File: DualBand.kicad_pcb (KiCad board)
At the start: 2 copper layers, 70.4 x 42.6 mm, 47 parts, among them J1 Conn_01x02_Male, J2 Conn_01x03_Male, J3 Conn_01x01_Male, J4 Conn_01x10_Male, J5 Conn_01x03_Male, J6 Conn_01x10_Male, J7 Conn_01x03_Male, P2 AD8402ARUZ1, SW1 SW_Push, U1 LM7322QMAX/NOPB, U2 MSP430FR2311IPW20R, U3 LMH6703MA/NOPB, U4 LMH6703MA/NOPB

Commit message: Generated Gerbers
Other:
- board text added: "Chris Dietsch & Lonnie Souder II"
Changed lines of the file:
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@@
-(kicad_pcb (version 4) (host pcbnew 4.0.7)
+(kicad_pcb (version 4) (host pcbnew 4.0.4-stable)
   (general
     (links 118)
     (no_connects 0)
-    (area 97.714999 97.953689 172.160001 167.8)
+    (area 97.79 98.053689 172.160001 167.8)
     (thickness 1.6)
-    (drawings 7)
+    (drawings 8)
     (tracks 718)
     (zones 0)
@@
     (visible_elements 7FFFFFFF)
     (pcbplotparams
-      (layerselection 0x00030_80000001)
-      (usegerberextensions false)
+      (layerselection 0x010f0_80000001)
+      (usegerberextensions true)
       (excludeedgelayer true)
       (linewidth 0.100000)
@@
       (psa4output false)
       (plotreference true)
-      (plotvalue true)
+      (plotvalue false)
       (plotinvisibletext false)
       (padsonsilk false)
@@
       (outputformat 1)
       (mirror false)
-      (drillshape 1)
+      (drillshape 0)
       (scaleselection 1)
       (outputdirectory ""))
@@
     )
   )
+  (gr_text "Chris Dietsch & Lonnie Souder II" (at 158.2 141.2) (layer F.SilkS)
+    (effects (font (size 1 1) (thickness 0.25)))
+  )
   (gr_line (start 101.6635 100.965) (end 172.085 100.965) (angle 90) (layer Edge.Cuts) (width 0.15))

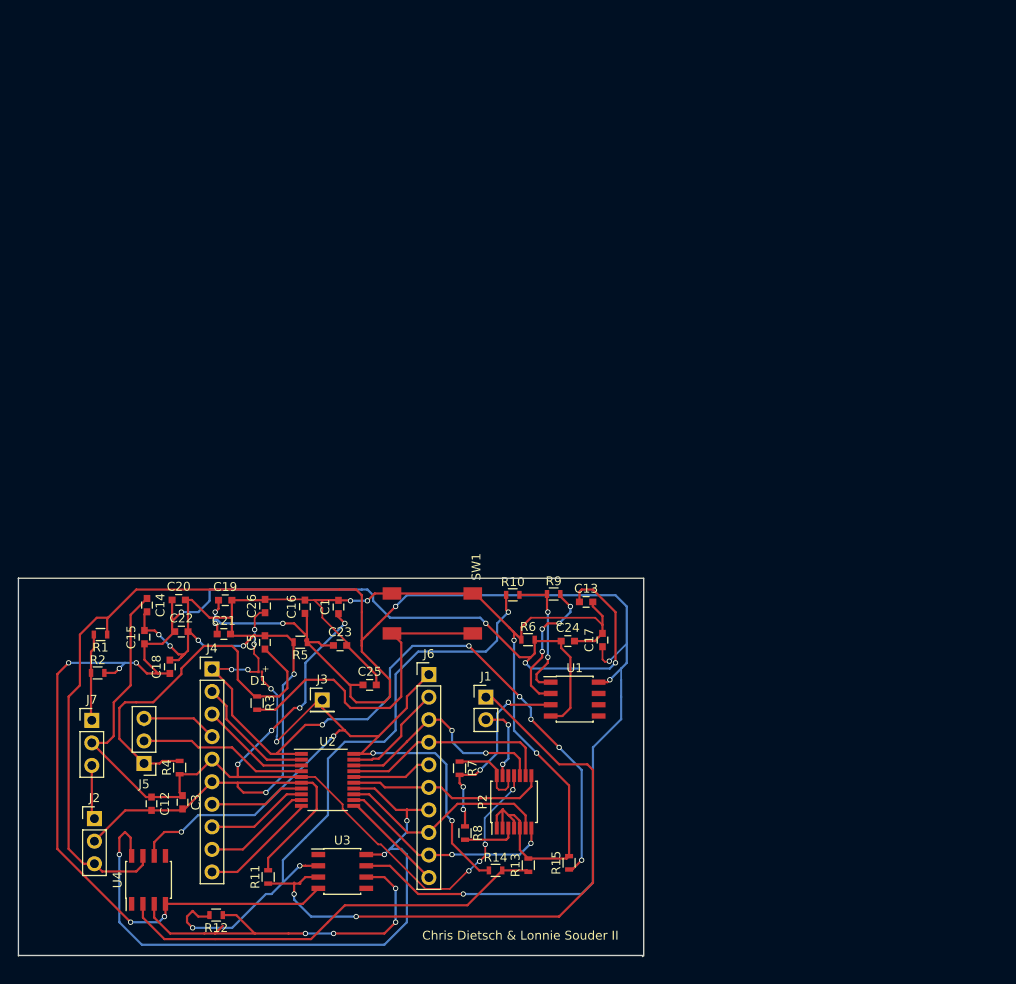
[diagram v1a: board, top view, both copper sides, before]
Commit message: Recreates PCB based on new layout
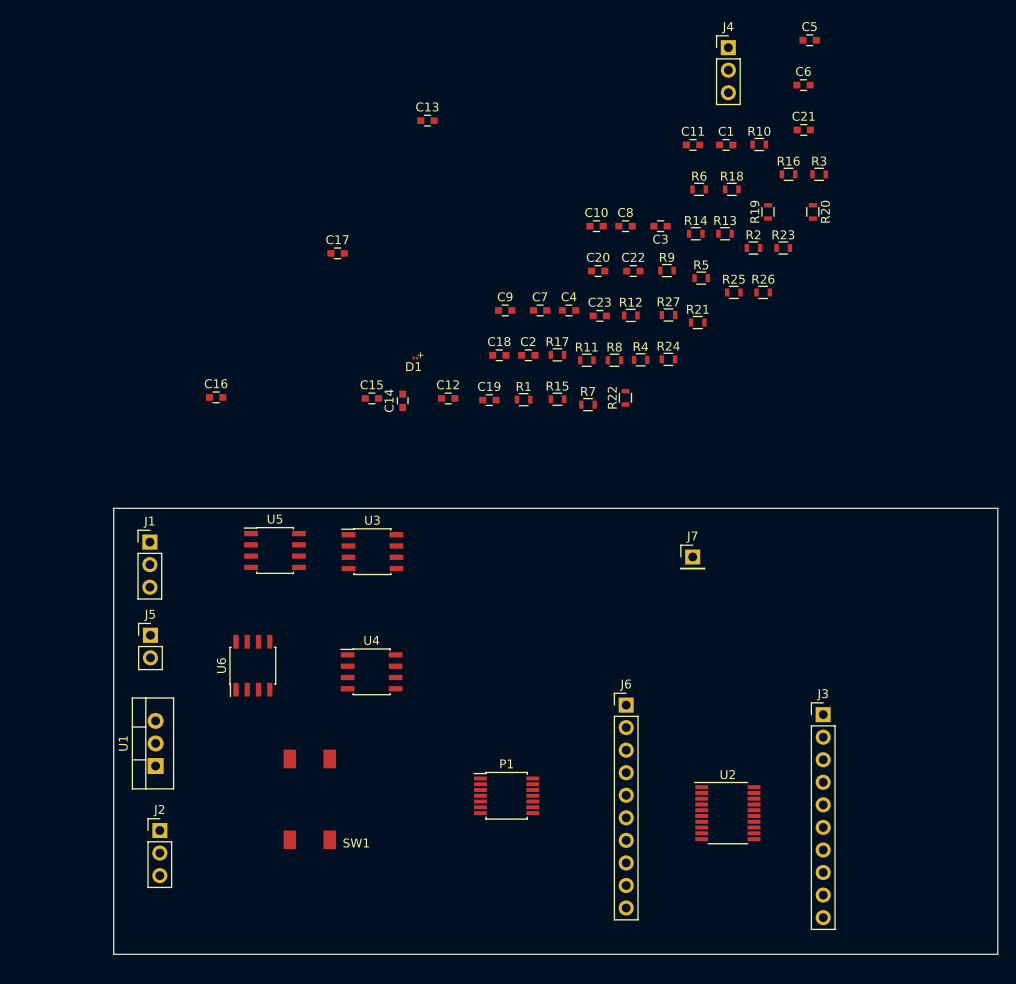
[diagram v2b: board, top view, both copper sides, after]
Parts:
- removed C24, C25: 0.01u, Capacitors_SMD:C_0603
- removed C26: 0.1u, Capacitors_SMD:C_0603
- removed P2: AD8402ARUZ1, Housings_SSOP:TSSOP-14_4.4x5mm_Pitch0.65mm
- added C10: 1u, Capacitors_SMD:C_0603, F.Cu at (166.8, 61.3)
- added C11: 1u, Capacitors_SMD:C_0603, F.Cu at (177.6, 52.2)
- added C2: 1u, Capacitors_SMD:C_0603, F.Cu at (159.1, 75.9)
- added C4: 10u, Capacitors_SMD:C_0603, F.Cu at (163.7, 70.8)
- added C6: 1u, Capacitors_SMD:C_0603, F.Cu at (190.1, 45.4)
- added C7: 1u, Capacitors_SMD:C_0603, F.Cu at (160.4, 70.8)
- added C8: 1u, Capacitors_SMD:C_0603, F.Cu at (170.0, 61.3)
- added C9: 0.01u, Capacitors_SMD:C_0603, F.Cu at (156.5, 70.8)
- added P1: AD8402ARUZ1, Housings_SSOP:TSSOP-14_4.4x5mm_Pitch0.65mm, F.Cu at (156.6, 125.5)
- added R16: 820, Resistors_SMD:R_0603, F.Cu at (188.4, 55.5)
- added R17: 10k, Resistors_SMD:R_0603, F.Cu at (162.4, 75.8)
- added R18: 100, Resistors_SMD:R_0603, F.Cu at (182.0, 57.2)
- added R19: 10k, Resistors_SMD:R_0603, F.Cu at (186.1, 59.7)
- added R20: 1k, Resistors_SMD:R_0603, F.Cu at (191.1, 59.7)
- added R21: 1k, Resistors_SMD:R_0603, F.Cu at (178.2, 72.2)
- added R22: 287, Resistors_SMD:R_0603, F.Cu at (170.0, 80.6)
- added R23: 2.4k, Resistors_SMD:R_0603, F.Cu at (187.8, 63.8)
- added R24: 470, Resistors_SMD:R_0603, F.Cu at (174.9, 76.3)
- added R25: 100, Resistors_SMD:R_0603, F.Cu at (182.2, 68.8)
- added R26: 220, Resistors_SMD:R_0603, F.Cu at (185.5, 68.8)
- added R27: 10k, Resistors_SMD:R_0603, F.Cu at (174.9, 71.3)
- added U5: LMH6703MA/NOPB, Housings_SOIC:SOIC-8_3.9x4.9mm_Pitch1.27mm, F.Cu at (130.6, 97.8)
- added U6: LMH6703MA/NOPB, Housings_SOIC:SOIC-8_3.9x4.9mm_Pitch1.27mm, F.Cu at (128.1, 110.8)
- C1: value 1u -> 100n
- C12, C19, C22: value 1u -> 0.01u
- C15, C17, C20, C21: value 0.01u -> 1u
- C23: value 1u -> 0.1u
- J1: value Conn_01x02_Male -> Conn_01x03_Male; footprint Pin_Headers:Pin_Header_Straight_1x02_Pitch2.54mm -> Pin_Headers:Pin_Header_Straight_1x03_Pitch2.54mm
- J3: value Conn_01x01_Male -> Conn_01x10_Male; footprint Pin_Headers:Pin_Header_Straight_1x01_Pitch2.54mm -> Pin_Headers:Pin_Header_Straight_1x10_Pitch2.54mm
- J4: value Conn_01x10_Male -> Conn_01x03_Male; footprint Pin_Headers:Pin_Header_Straight_1x10_Pitch2.54mm -> Pin_Headers:Pin_Header_Straight_1x03_Pitch2.54mm
- J5: value Conn_01x03_Male -> Conn_01x02_Male; footprint Pin_Headers:Pin_Header_Straight_1x03_Pitch2.54mm -> Pin_Headers:Pin_Header_Straight_1x02_Pitch2.54mm
- J7: value Conn_01x03_Male -> Conn_01x01_Male; footprint Pin_Headers:Pin_Header_Straight_1x03_Pitch2.54mm -> Pin_Headers:Pin_Header_Straight_1x01_Pitch2.54mm
- R1: value 12k -> 10k
- R10: value 100 -> 10
- R11: value 75 -> 10
- R12: value 287 -> 24k
- R13: value 100 -> 24k
- R14: value 220 -> 250
- R15: value 10k -> 820
- R2: value 78.7k -> 10k
- R3: value 10k -> 3.9k
- R4: value 10k -> 1k
- R5, R6: value 10k -> 510k
- R7: value 3k -> 1.3k
- R8: value 10 -> R
- R9: value 250 -> R
- U1: value LM7322QMAX/NOPB -> LD1117V33; footprint Housings_SOIC:SOIC-8_3.9x4.9mm_Pitch1.27mm -> TO_SOT_Packages_THT:TO-220-3_Vertical
- moved C5 91.5 mm to (190.8, 40.4), turned to 0 degrees
- moved J4 91.0 mm to (181.6, 41.2)
- moved R2 88.0 mm to (184.5, 63.8)
- moved R3 86.9 mm to (191.8, 55.5), turned to 0 degrees
- moved C21 86.5 mm to (190.1, 50.5)
- moved C3 84.3 mm to (174.0, 61.3), turned to 180 degrees
- moved R12 82.1 mm to (170.6, 71.4), turned to 0 degrees
- moved R14 75.2 mm to (177.9, 62.2)
- moved R13 74.5 mm to (181.2, 62.2), turned to 0 degrees
- moved J7 70.1 mm to (177.6, 98.6)
- moved R4 69.3 mm to (171.7, 76.4), turned to 0 degrees
- moved R11 68.4 mm to (165.7, 76.4), turned to 0 degrees
- moved C1 67.9 mm to (181.4, 52.2), turned to 0 degrees
- moved C22 65.1 mm to (170.9, 66.4)
- moved R5 61.0 mm to (178.6, 67.2), turned to 0 degrees
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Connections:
- C1 pad 1: /DVCC -> +9V
- C13 pad 1: /-4.5V -> +9V
- C14 pad 1: /DVCC -> +9V
- C15 pad 1: /-4.5V -> Net-(C15-Pad1)
- C15 pad 2: GND -> Net-(C15-Pad2)
- C16 pad 1: +9V -> Net-(C16-Pad1)
- C16 pad 2: GND -> /DataSignalIn
- C17 pad 1: +9V -> Net-(C17-Pad1)
- C18 pad 1: /-4.5V -> +9V
- C20 pad 1: /-4.5V -> Net-(C20-Pad1)
- C20 pad 2: GND -> Net-(C20-Pad2)
- C22 pad 1: /-4.5V -> +9V
- C23 pad 1: +9V -> Net-(C23-Pad1)
- C3 pad 2: GND -> Net-(C3-Pad2)
- D1 pad 1: Net-(C26-Pad1) -> Net-(C23-Pad1)
- J1 pad 1: /DataSignalIn -> +3V3
- J1 pad 2: /PowerSignalIn -> GND
- J2 pad 1: +3V3 -> Net-(C4-Pad1)
- J2 pad 2: GND -> /DVCC
- J2 pad 3: +9V -> +3V3
- J3 pad 1: /DataOut -> Net-(C23-Pad1)
- J4 pad 1: Net-(C26-Pad1) -> Net-(C5-Pad1)
- J4 pad 3: Net-(J4-Pad3) -> Net-(J3-Pad4)
- J5 pad 1: Net-(C5-Pad1) -> /DataSignalIn
- J7 pad 1: Net-(J7-Pad1) -> /DataOut
- R1 pad 1: +9V -> Net-(C5-Pad1)
- R1 pad 2: Net-(J7-Pad1) -> Net-(R1-Pad2)
- R10 pad 1: Net-(R10-Pad1) -> Net-(P1-Pad12)
- R10 pad 2: Net-(R10-Pad2) -> Net-(C11-Pad2)
- R11 pad 1: /DataSignalIn -> Net-(C11-Pad2)
- R11 pad 2: GND -> Net-(P1-Pad3)
- R12 pad 1: Net-(R12-Pad1) -> +9V
- R12 pad 2: Net-(R10-Pad1) -> Net-(C11-Pad1)
- R13 pad 1: Net-(R13-Pad1) -> Net-(C11-Pad1)
- R14 pad 1: /DataOut -> Net-(C15-Pad2)
- R14 pad 2: Net-(R13-Pad1) -> Net-(R14-Pad2)
- R15 pad 1: Net-(C26-Pad1) -> +9V
- R15 pad 2: GND -> Net-(C15-Pad1)
- R2 pad 1: Net-(J7-Pad1) -> /DVCC
- R2 pad 2: /-4.5V -> Net-(C5-Pad1)
- R3 pad 1: Net-(C5-Pad1) -> Net-(J5-Pad2)
- R3 pad 2: Net-(R3-Pad2) -> Net-(C6-Pad2)
- R4 pad 1: /DVCC -> Net-(C6-Pad2)
- R4 pad 2: Net-(C5-Pad1) -> GND
- R5 pad 2: GND -> Net-(C6-Pad1)
- R6 pad 1: GND -> Net-(C6-Pad1)
- R6 pad 2: /-4.5V -> GND
- R7 pad 1: Net-(P2-Pad12) -> Net-(C8-Pad2)
- R8 pad 1: Net-(R7-Pad2) -> +9V
- R8 pad 2: Net-(P2-Pad3) -> Net-(C8-Pad1)
- R9 pad 1: Net-(R10-Pad2) -> Net-(C8-Pad1)
- R9 pad 2: Net-(R9-Pad2) -> GND
- SW1 pad 2: Net-(R3-Pad2) -> Net-(R1-Pad2)
- U1 pad 1: Net-(R10-Pad2) -> GND
- U1 pad 2: Net-(R9-Pad2) -> Net-(C4-Pad1)
- U1 pad 3: Net-(R7-Pad2) -> +9V
- U2 pad 1: Net-(C26-Pad1) -> Net-(C23-Pad1)
- U2 pad 10: Net-(J4-Pad10) -> Net-(J3-Pad10)
- U2 pad 2: Net-(J4-Pad2) -> Net-(J3-Pad2)
- U2 pad 3: Net-(J4-Pad3) -> Net-(J3-Pad3)
- U2 pad 4: Net-(J5-Pad2) -> Net-(J4-Pad2)
- U2 pad 7: Net-(J4-Pad7) -> Net-(J3-Pad7)
- U2 pad 8: Net-(J4-Pad8) -> Net-(J3-Pad8)
- U2 pad 9: Net-(J4-Pad9) -> Net-(J3-Pad9)
- U3 pad 2: Net-(R10-Pad1) -> Net-(R7-Pad2)
- U3 pad 3: /DataSignalIn -> Net-(C6-Pad1)
- U3 pad 4: /-4.5V -> GND
- U3 pad 6: Net-(R12-Pad1) -> Net-(C8-Pad2)
- U4 pad 2: Net-(R13-Pad1) -> Net-(R14-Pad2)
- U4 pad 3: Net-(R12-Pad1) -> Net-(C11-Pad1)
- U4 pad 4: /-4.5V -> GND
- U4 pad 6: /DataOut -> Net-(C15-Pad2)
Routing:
- net +9V: track 222.5 -> 0.00 mm, vias 7 -> 0
- net GND: track 219.5 -> 0.00 mm, vias 10 -> 0
- net /-4.5V: track 168.8 -> 0.00 mm, vias 9 -> 0
- net /DVCC: track 112.7 -> 0.00 mm, vias 8 -> 0
- net /DataOut: track 91.0 -> 0.00 mm, vias 6 -> 0
- net Net-(C26-Pad1): track 88.6 -> 0.00 mm, vias 10 -> 0
- net /~SD: track 75.4 -> 0.00 mm, vias 3 -> 0
- net /DataSignalIn: track 72.4 -> 0.00 mm, vias 2 -> 0
- net Net-(R10-Pad1): track 71.8 -> 0.00 mm, vias 3 -> 0
- net Net-(R13-Pad1): track 49.2 -> 0.00 mm
- net Net-(R12-Pad1): track 44.1 -> 0.00 mm, vias 4 -> 0
- net Net-(C5-Pad1): track 43.8 -> 0.00 mm
- net Net-(R3-Pad2): track 37.0 -> 0.00 mm
- net Net-(J6-Pad3): track 25.3 -> 0.00 mm, vias 2 -> 0
- net Net-(J6-Pad9): track 24.8 -> 0.00 mm, vias 2 -> 0
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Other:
- board size 70.4 x 42.6 mm -> 99.6 x 50.2 mm
- net class Default: clearance 0.1 -> 0.2; trace_width 0.2 -> 0.25
- net class Diode removed
- rule trace_clearance: 0.1 -> 0.2
- board text removed: "Chris Dietsch & Lonnie Souder II"

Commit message: Revised PCB
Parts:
- added C24: 1u, Capacitors_SMD:C_0603, F.Cu at (138.4, 113.5)
- moved J4 96.8 mm to (164.8, 136.6), turned to 270 degrees
- moved R3 89.4 mm to (122.7, 112.1)
- moved R10 77.5 mm to (163.8, 126.7), turned to 270 degrees
- moved R20 74.4 mm to (167.6, 130.3)
- moved C3 74.3 mm to (155.6, 133.3)
- moved R6 74.2 mm to (165.7, 130.3), turned to 90 degrees
- moved C4 70.8 mm to (117.8, 124.8)
- moved C21 70.4 mm to (155.3, 111.7), turned to 270 degrees
- moved C10 70.1 mm to (155.7, 130.5), turned to 180 degrees
- moved R2 68.1 mm to (158.5, 126.8), turned to 90 degrees
- moved R26 68.0 mm to (158.8, 131.3), turned to 270 degrees
- moved R19 66.8 mm to (163.2, 122.5), turned to 180 degrees
- moved C5 66.8 mm to (159.4, 99.4), turned to 90 degrees
- moved C6 66.7 mm to (166.2, 107.7), turned to 270 degrees
- moved R25 65.0 mm to (161.2, 130.3), turned to 90 degrees
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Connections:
- C3 pad 2: Net-(C3-Pad2) -> GND
- R26 pad 1: /DataOut -> Net-(C24-Pad2)
- U6 pad 6: /DataOut -> Net-(C24-Pad2)
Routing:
- net GND: track 0.00 -> 219.4 mm, vias 0 -> 15
- net +9V: track 0.00 -> 138.3 mm, vias 0 -> 13
- net Net-(C17-Pad1): track 0.00 -> 131.8 mm, vias 0 -> 8
- net Net-(J6-Pad8): track 0.00 -> 117.4 mm, vias 0 -> 4
- net Net-(C6-Pad2): track 0.00 -> 116.4 mm, vias 0 -> 8
- net Net-(C8-Pad1): track 0.00 -> 109.1 mm, vias 0 -> 4
- net /DVCC: track 0.00 -> 91.7 mm, vias 0 -> 8
- net Net-(C6-Pad1): track 0.00 -> 80.9 mm, vias 0 -> 6
- net Net-(J6-Pad3): track 0.00 -> 65.9 mm, vias 0 -> 3
- net Net-(C11-Pad1): track 0.00 -> 63.4 mm, vias 0 -> 6
- net /~SD: track 0.00 -> 62.7 mm, vias 0 -> 4
- net Net-(C23-Pad1): track 0.00 -> 61.0 mm, vias 0 -> 4
- net Net-(R17-Pad1): track 0.00 -> 55.9 mm, vias 0 -> 6
- net Net-(C15-Pad1): track 0.00 -> 48.5 mm, vias 0 -> 4
- net Net-(C5-Pad1): track 0.00 -> 47.0 mm, vias 0 -> 6
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- added copper zone on B.Cu, net GND
- added copper zone on F.Cu, net GND
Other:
- board size 99.6 x 50.2 mm -> 68.5 x 53 mm
- net class Default: clearance 0.2 -> 0.05
- net class Large added: clearance 0.05, trace_width 0.45, via_dia 0.6, via_drill 0.45
- rule trace_clearance: 0.2 -> 0.05
- board text added: "Circuit Design by Lonnie Souder II Layout by Chris Dietsch"
